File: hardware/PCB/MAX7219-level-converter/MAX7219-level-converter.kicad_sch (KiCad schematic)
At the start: 4 parts, among them U1 SN74LV1T34DBV, U2 MAX7219, U3 SN74LV1T34DBV, U4 SN74LV1T34DBV

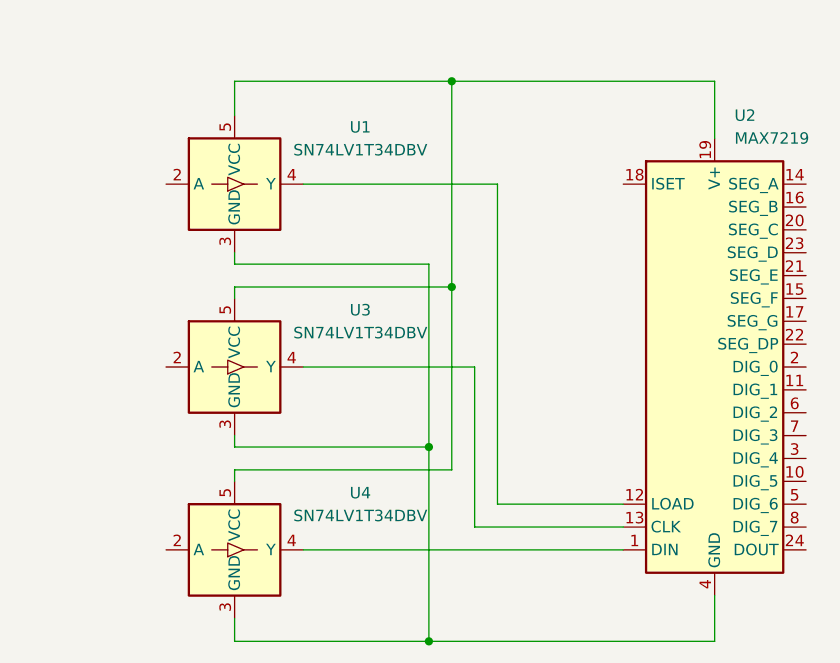
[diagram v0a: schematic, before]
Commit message: signal level converter for new hardware version 1.0
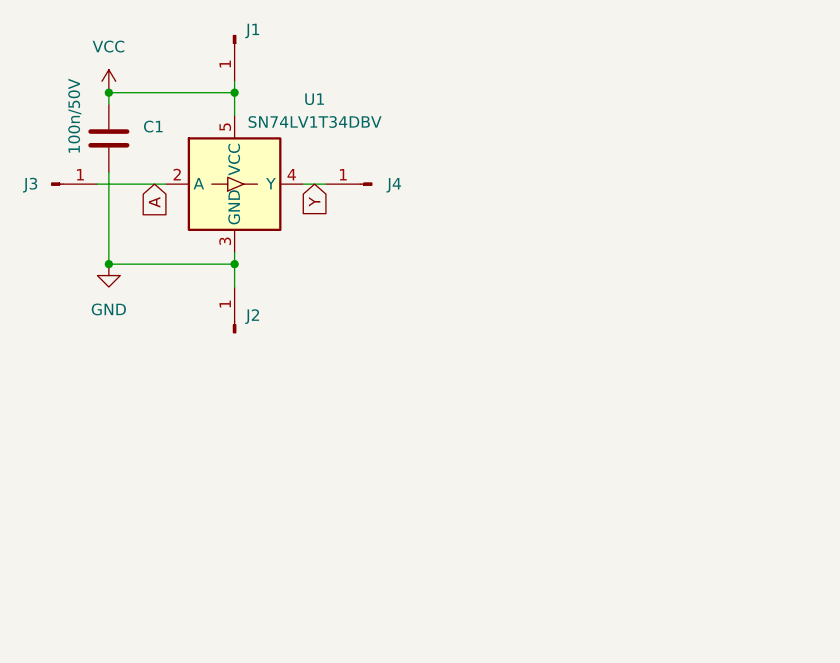
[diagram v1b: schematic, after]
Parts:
- removed U2: MAX7219, MAX7219:MAX7219-pigipack, symbol Driver_LED:MAX7219
- removed U3, U4: SN74LV1T34DBV, Package_TO_SOT_SMD:SOT-23-5, symbol Logic_LevelTranslator:SN74LV1T34DBV
- added C1: 100n/50V, Capacitor_SMD:C_0603_1608Metric_Pad1.08x0.95mm_HandSolder, symbol Device:C
- added J1: VCC, Connector_Wire:SolderWirePad_1x01_SMD_1x2mm, symbol Connector:Conn_01x01_Pin
- added J2: GND, Connector_Wire:SolderWirePad_1x01_SMD_1x2mm, symbol Connector:Conn_01x01_Pin
- added J3, J4: Conn_01x01_Pin, Connector_Wire:SolderWirePad_1x01_SMD_1x2mm, symbol Connector:Conn_01x01_Pin
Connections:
- net GND: now reaches U1.3 (GND)
- net GND: now also C1.2, J2.1 (Pin_1)
- net VCC: now reaches U1.5 (VCC)
- net VCC: now also C1.1, J1.1 (Pin_1)
- net A: now reaches U1.2 (A)
- net A: now also J3.1 (Pin_1)
- net Y: now reaches U1.4 (Y)
- net Y: now also J4.1 (Pin_1)
